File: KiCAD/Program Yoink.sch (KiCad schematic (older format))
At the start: 123 parts, among them SW1 Rotary_Encoder_Switch, SW2 SW_Push, U1 ATmega32U2-AU, U2 PRTR5V0U2X, Y1 Crystal_GND24_Small

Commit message: Updated Symbol lib path
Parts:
- U2: symbol random-keyboard-parts:PRTR5V0U2X -> Program-Yoink-rescue:PRTR5V0U2X-random-keyboard-parts
- USB1: symbol Type-C:HRO-TYPE-C-31-M-12 -> Program-Yoink-rescue:HRO-TYPE-C-31-M-12-Type-C
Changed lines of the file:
@@
 EESchema Schematic File Version 4
-LIBS:Program Yoink-cache
 EELAYER 30 0
 EELAYER END
@@
 EncS2
 $Comp
-L Type-C:HRO-TYPE-C-31-M-12 USB1
+L Program-Yoink-rescue:HRO-TYPE-C-31-M-12-Type-C USB1
 U 1 1 5F7EBCC9
 P 6200 8700
@@
 D+
 $Comp
-L random-keyboard-parts:PRTR5V0U2X U2
+L Program-Yoink-rescue:PRTR5V0U2X-random-keyboard-parts U2
 U 1 1 5F89C082
 P 7250 9050

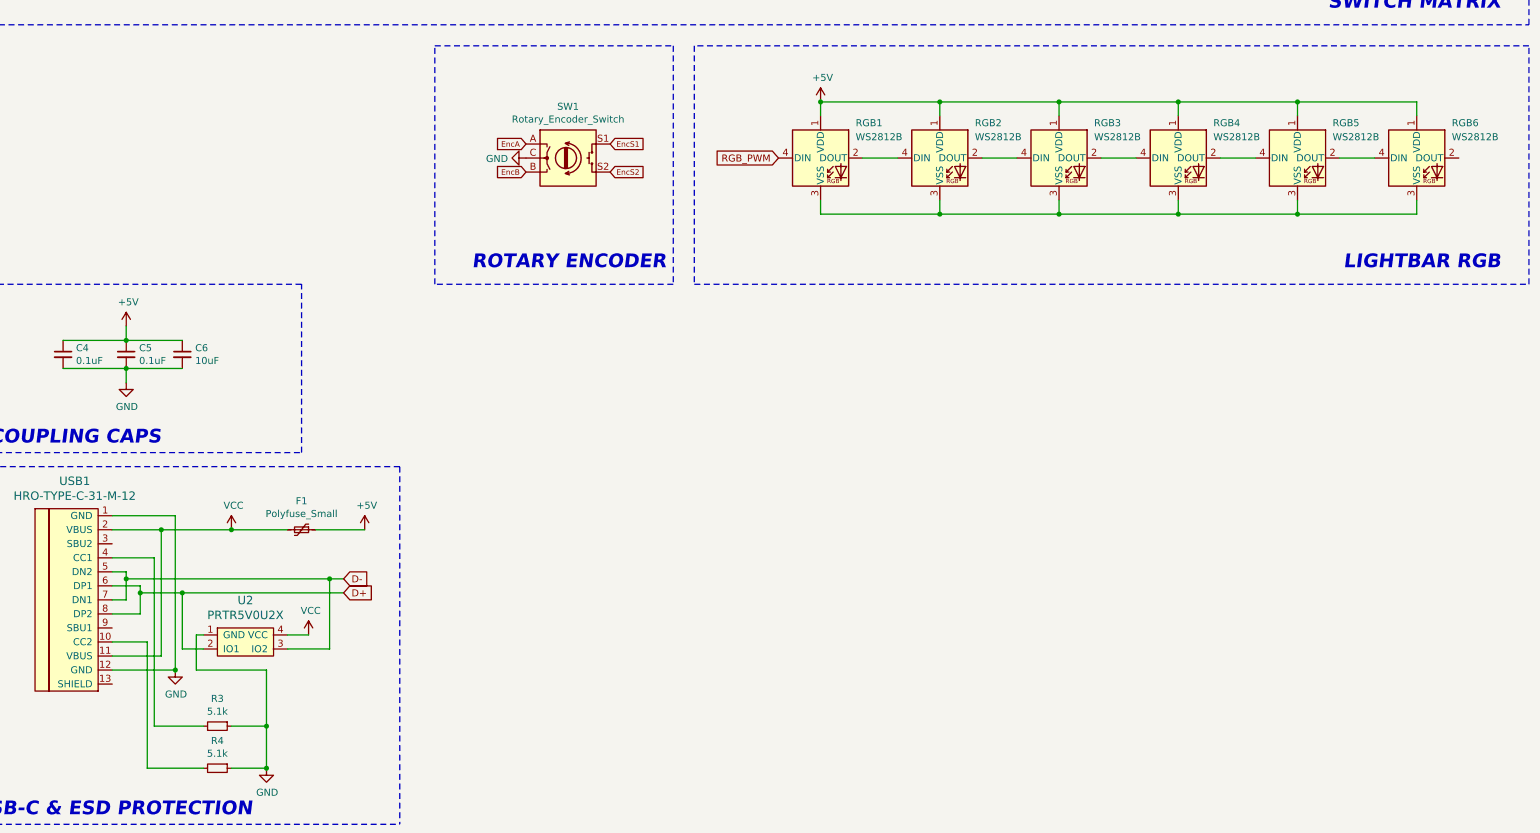
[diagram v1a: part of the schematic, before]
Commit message: Fixed LED gnd
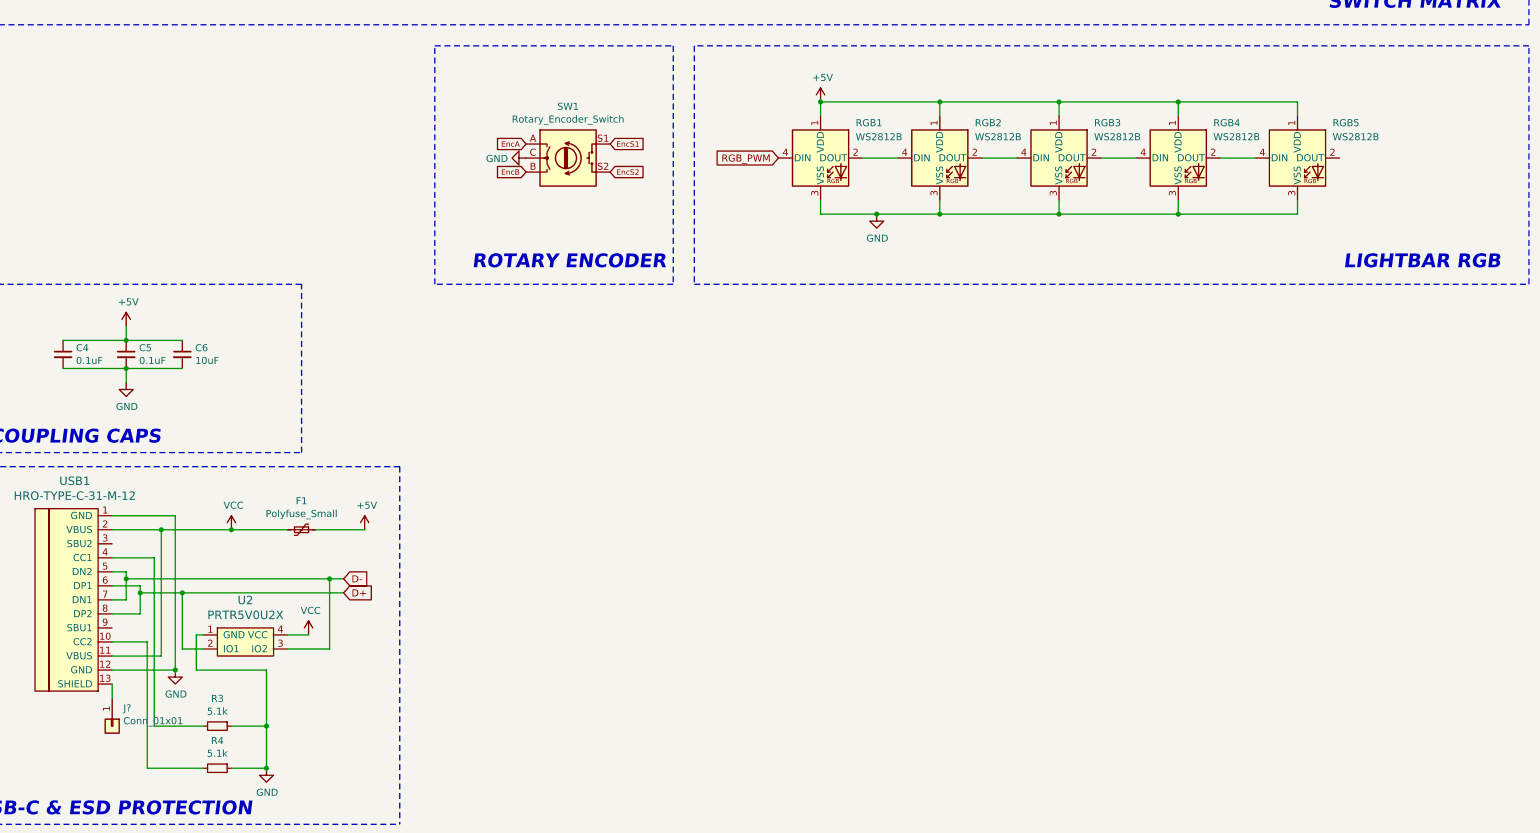
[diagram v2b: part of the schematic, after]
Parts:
- removed RGB6: WS2812B, LED_SMD:LED_WS2812B_PLCC4_5.0x5.0mm_P3.2mm, symbol LED:WS2812B
- added J?: Conn_01x01, symbol Connector_Generic:Conn_01x01
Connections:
- net GND: now also RGB1.3 (VSS), RGB2.3 (VSS), RGB3.3 (VSS), RGB4.3 (VSS), RGB5.3 (VSS)
- net at USB1.13 (SHIELD): now also J?.1 (Pin_1)
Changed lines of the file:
@@
 	13050 5900 13050 6000
 Wire Wire Line
-	11350 6000 12200 6000
+	11350 6000 11750 6000
 Connection ~ 13050 6000
 Wire Wire Line
@@
 	1    0    0    -1
 $EndComp
-$Comp
-L LED:WS2812B RGB6
-U 1 1 5F8B255C
-P 15600 5600
-F 0 "RGB6" H 15850 5850 50  0000 L CNN
-F 1 "WS2812B" H 15850 5750 50  0000 L CNN
-F 2 "LED_SMD:LED_WS2812B_PLCC4_5.0x5.0mm_P3.2mm" H 15650 5300 50  0001 L TNN
-F 3 "https://cdn-shop.adafruit.com/datasheets/WS2812B.pdf" H 15700 5225 50  0001 L TNN
-	1    15600 5600
-	1    0    0    -1
-$EndComp
 Wire Wire Line
 	14200 5600 14450 5600
-Wire Wire Line
-	15050 5600 15300 5600
-Wire Wire Line
-	15600 5300 15600 5200
-Wire Wire Line
-	15600 5200 14750 5200
 Connection ~ 13900 5200
 Wire Wire Line
 	14750 5300 14750 5200
-Connection ~ 14750 5200
 Wire Wire Line
 	14750 5200 13900 5200
 Wire Wire Line
 	13900 6000 14750 6000
-Wire Wire Line
-	15600 6000 15600 5900
 Connection ~ 13900 6000
 Wire Wire Line
 	14750 5900 14750 6000
-Connection ~ 14750 6000
-Wire Wire Line
-	14750 6000 15600 6000
 $Comp
 L power:+5V #PWR0101
@@
 Text GLabel 15550 1350 0    39   Input ~ 0
 EncS2
-$Comp
-L Program-Yoink-rescue:HRO-TYPE-C-31-M-12-Type-C USB1
-U 1 1 5F7EBCC9
-P 6200 8700
-F 0 "USB1" H 6033 9497 60  0000 C CNN
-F 1 "HRO-TYPE-C-31-M-12" H 6033 9391 60  0000 C CNN
-F 2 "Type-C:HRO-TYPE-C-31-M-12-HandSoldering" H 6200 8700 60  0001 C CNN
-F 3 "" H 6200 8700 60  0001 C CNN
-	1    6200 8700
-	1    0    0    -1
-$EndComp
 $Comp
 L power:VCC #PWR0112
@@
 Text Notes 10250 6400 2    98   Italic 20
 ROTARY ENCODER
+$Comp
+L Connector_Generic:Conn_01x01 J?
+U 1 1 5F875FAC
+P 6300 9650
+F 0 "J?" V 6172 9730 50  0000 L CNN
+F 1 "Conn_01x01" V 6263 9730 50  0000 L CNN
+F 2 "" H 6300 9650 50  0001 C CNN
+F 3 "~" H 6300 9650 50  0001 C CNN
+	1    6300 9650
+	0    1    1    0
+$EndComp
+$Comp
+L Program-Yoink-rescue:HRO-TYPE-C-31-M-12-Type-C USB1
+U 1 1 5F7EBCC9
+P 6200 8700
+F 0 "USB1" H 6033 9497 60  0000 C CNN
+F 1 "HRO-TYPE-C-31-M-12" H 6033 9391 60  0000 C CNN
+F 2 "Type-C:HRO-TYPE-C-31-M-12-HandSoldering" H 6200 8700 60  0001 C CNN
+F 3 "" H 6200 8700 60  0001 C CNN
+	1    6200 8700
+	1    0    0    -1
+$EndComp
+Wire Wire Line
+	6300 9350 6300 9450
+$Comp
+L power:GND #PWR?
+U 1 1 5F8BD8B4
+P 11750 6000
+F 0 "#PWR?" H 11750 5750 50  0001 C CNN
+F 1 "GND" H 11755 5827 50  0000 C CNN
+F 2 "" H 11750 6000 50  0001 C CNN
+F 3 "" H 11750 6000 50  0001 C CNN
+	1    11750 6000
+	1    0    0    -1
+$EndComp
+Connection ~ 11750 6000
+Wire Wire Line
+	11750 6000 12200 6000
 $EndSCHEMATC

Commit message: Updated traces
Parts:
- gave numbers to parts that had none: 1
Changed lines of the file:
@@
 Wire Wire Line
 	13050 5900 13050 6000
-Wire Wire Line
-	11350 6000 11750 6000
 Connection ~ 13050 6000
 Wire Wire Line
@@
 Wire Wire Line
 	12200 5900 12200 6000
-Connection ~ 12200 6000
 Wire Wire Line
 	12200 6000 13050 6000
@@
 ROTARY ENCODER
 $Comp
-L Connector_Generic:Conn_01x01 J?
+L Connector_Generic:Conn_01x01 J1
 U 1 1 5F875FAC
 P 6300 9650
-F 0 "J?" V 6172 9730 50  0000 L CNN
+F 0 "J1" V 6172 9730 50  0000 L CNN
 F 1 "Conn_01x01" V 6263 9730 50  0000 L CNN
 F 2 "" H 6300 9650 50  0001 C CNN
@@
 	6300 9350 6300 9450
 $Comp
-L power:GND #PWR?
+L power:GND #PWR0117
 U 1 1 5F8BD8B4
-P 11750 6000
-F 0 "#PWR?" H 11750 5750 50  0001 C CNN
-F 1 "GND" H 11755 5827 50  0000 C CNN
-F 2 "" H 11750 6000 50  0001 C CNN
-F 3 "" H 11750 6000 50  0001 C CNN
-	1    11750 6000
-	1    0    0    -1
-$EndComp
-Connection ~ 11750 6000
-Wire Wire Line
-	11750 6000 12200 6000
+P 11350 6000
+F 0 "#PWR0117" H 11350 5750 50  0001 C CNN
+F 1 "GND" H 11355 5827 50  0000 C CNN
+F 2 "" H 11350 6000 50  0001 C CNN
+F 3 "" H 11350 6000 50  0001 C CNN
+	1    11350 6000
+	1    0    0    -1
+$EndComp
+Wire Wire Line
+	12200 6000 11350 6000
+Connection ~ 12200 6000
+Connection ~ 11350 6000
 $EndSCHEMATC

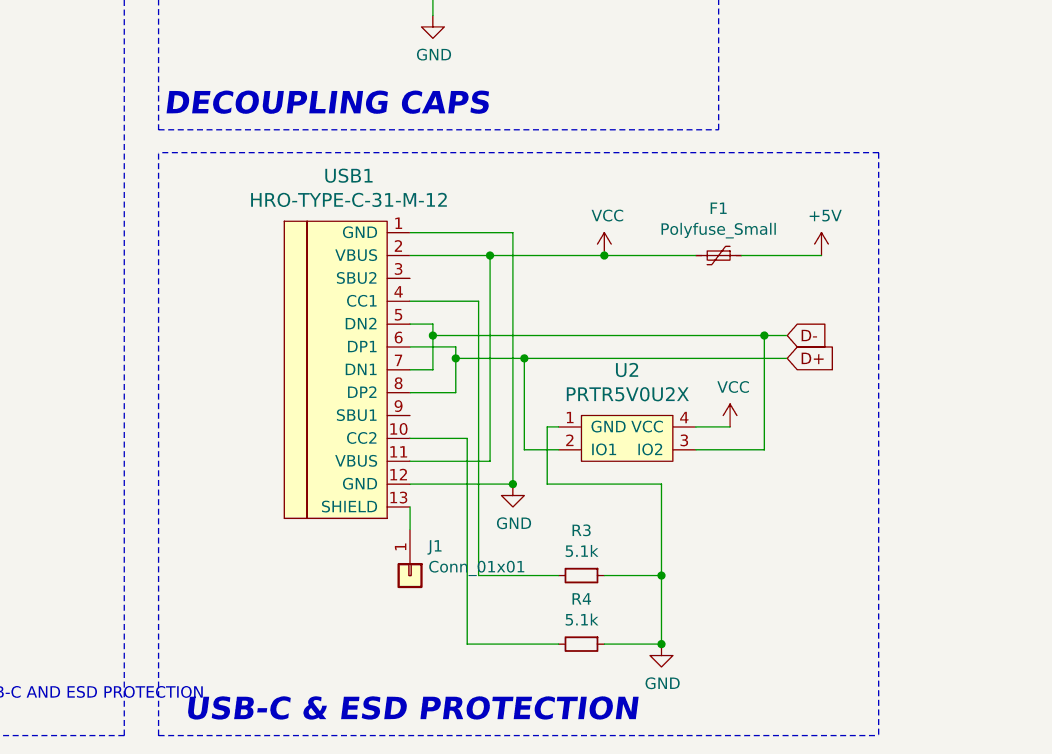
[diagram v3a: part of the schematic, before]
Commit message: Updated PCB
Added resistors to data lines
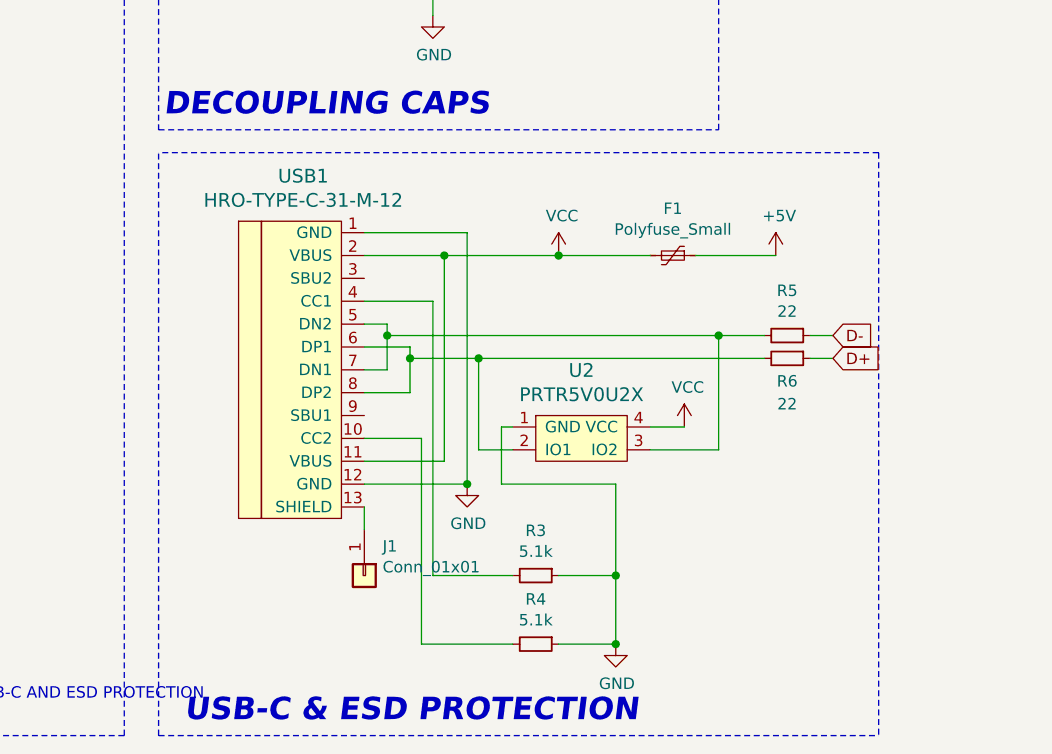
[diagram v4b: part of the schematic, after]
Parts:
- added R5, R6: 22, Resistor_SMD:R_0805_2012Metric, symbol Device:R_Small
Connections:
- net D+: now also R6.1; no longer U2.2 (IO1), USB1.6 (DP1), USB1.8 (DP2)
- net D-: now also R5.1; no longer U2.3 (IO2), USB1.5 (DN2), USB1.7 (DN1)
- new net: R5.2, U2.3 (IO2), USB1.5 (DN2), USB1.7 (DN1)
- new net: R6.2, U2.2 (IO1), USB1.6 (DP1), USB1.8 (DP2)
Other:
- moved on the sheet: F1, J1, R3, R4, U2, USB1

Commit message: Prepared production files
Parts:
- USB1: footprint Type-C:HRO-TYPE-C-31-M-12-HandSoldering -> Type-C:HRO-TYPE-C-31-M-12-Assembly
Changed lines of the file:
@@
 F 0 "USB1" H 5833 9497 60  0000 C CNN
 F 1 "HRO-TYPE-C-31-M-12" H 5833 9391 60  0000 C CNN
-F 2 "Type-C:HRO-TYPE-C-31-M-12-HandSoldering" H 6000 8700 60  0001 C CNN
+F 2 "Type-C:HRO-TYPE-C-31-M-12-Assembly" H 6000 8700 60  0001 C CNN
 F 3 "" H 6000 8700 60  0001 C CNN
 	1    6000 8700
